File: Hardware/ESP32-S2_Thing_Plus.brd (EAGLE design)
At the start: 22.9 x 64.8 mm, 144 parts, among them J3 QWIIC_RA, J5 USB-C, J6 JTAG, Q1 2.5A/30V, Q2 MBT3904DW1T1, U1 ESP32-S2-WROOM, U2 CP210X, U3 AP2112K-3.3V, U4 MCP73831, U5 TC7USB40MU, Y1 32.768kHz

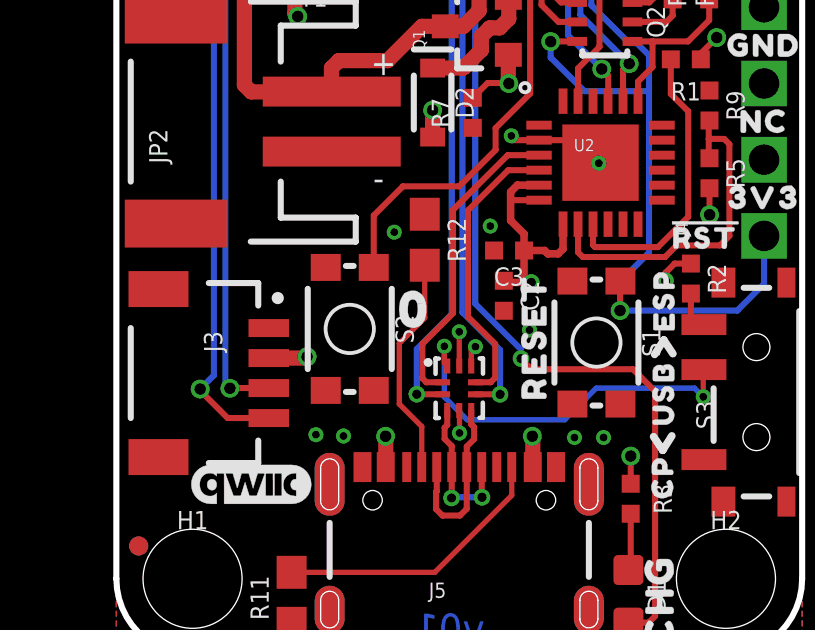
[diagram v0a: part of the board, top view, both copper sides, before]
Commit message: corrected extra IO sch note, moved "0" button to align with reset.
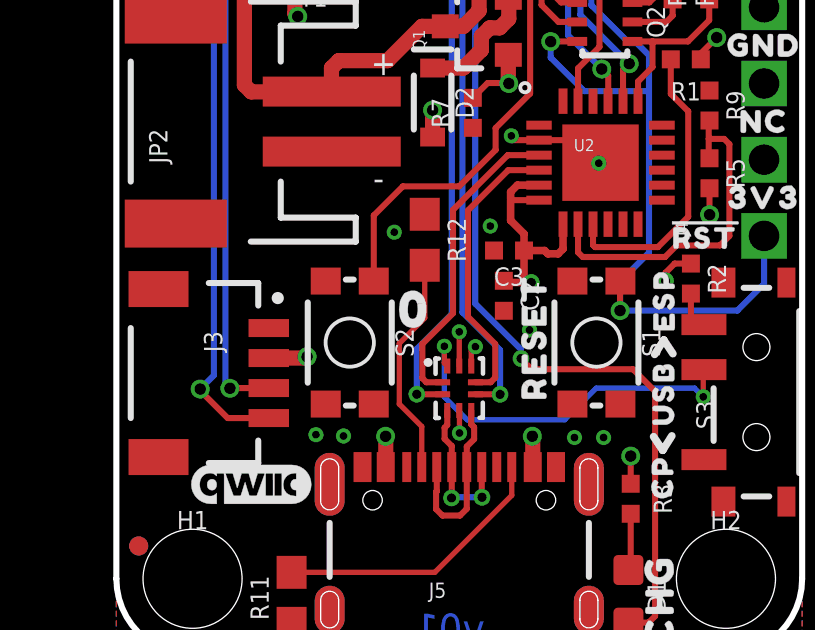
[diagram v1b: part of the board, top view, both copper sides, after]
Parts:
- moved S2 0.45 mm to (7.78, 10.4)
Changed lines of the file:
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@@
 <element name="FD3" library="SparkFun-Aesthetics" package="FIDUCIAL-MICRO" value="FIDUCIALUFIDUCIAL" x="0.74421875" y="3.634740625" smashed="yes"/>
 <element name="FD4" library="SparkFun-Aesthetics" package="FIDUCIAL-MICRO" value="FIDUCIALUFIDUCIAL" x="0.74421875" y="3.634740625" smashed="yes" rot="MR0"/>
-<element name="S2" library="SparkFun-Switches" package="TACTILE_SWITCH_SMD_4.6X2.8MM" value="0" x="7.78001875" y="10.868659375" smashed="yes" rot="R270">
-<attribute name="NAME" x="9.30401875" y="10.868659375" size="0.6096" layer="25" font="vector" ratio="20" rot="R270" align="bottom-center"/>
-<attribute name="PROD_ID" value="SWCH-13065" x="7.78001875" y="10.868659375" size="1.778" layer="27" rot="R270" display="off"/>
-<attribute name="VALUE" x="6.25601875" y="10.868659375" size="0.6096" layer="27" font="vector" ratio="20" rot="R270" align="top-center"/>
+<element name="S2" library="SparkFun-Switches" package="TACTILE_SWITCH_SMD_4.6X2.8MM" value="0" x="7.78001875" y="10.414" smashed="yes" rot="R270">
+<attribute name="NAME" x="9.30401875" y="10.414" size="0.6096" layer="25" font="vector" ratio="20" rot="R270" align="bottom-center"/>
+<attribute name="PROD_ID" value="SWCH-13065" x="7.78001875" y="10.414" size="1.778" layer="27" rot="R270" display="off"/>
+<attribute name="VALUE" x="6.25601875" y="10.414" size="0.6096" layer="27" font="vector" ratio="20" rot="R270" align="top-center"/>
 </element>
 <element name="TP1" library="SparkFun-Connectors" package="TP_15TH" value="" x="17.78" y="24.13" smashed="yes"/>
@@
 <wire x1="11.4274625" y1="15.621" x2="9.5504" y2="15.621" width="0.2032" layer="1"/>
 <wire x1="9.5504" y1="15.621" x2="8.58001875" y2="14.65061875" width="0.2032" layer="1"/>
-<wire x1="8.58001875" y1="14.65061875" x2="8.58001875" y2="12.918659375" width="0.2032" layer="1"/>
+<wire x1="8.58001875" y1="14.65061875" x2="8.58001875" y2="12.464" width="0.2032" layer="1"/>
 <wire x1="13.7922" y1="23.3934" x2="13.7922" y2="18.714721875" width="0.2032" layer="1"/>
 <wire x1="13.7922" y1="18.714721875" x2="12.64158125" y2="17.564103125" width="0.2032" layer="1"/>

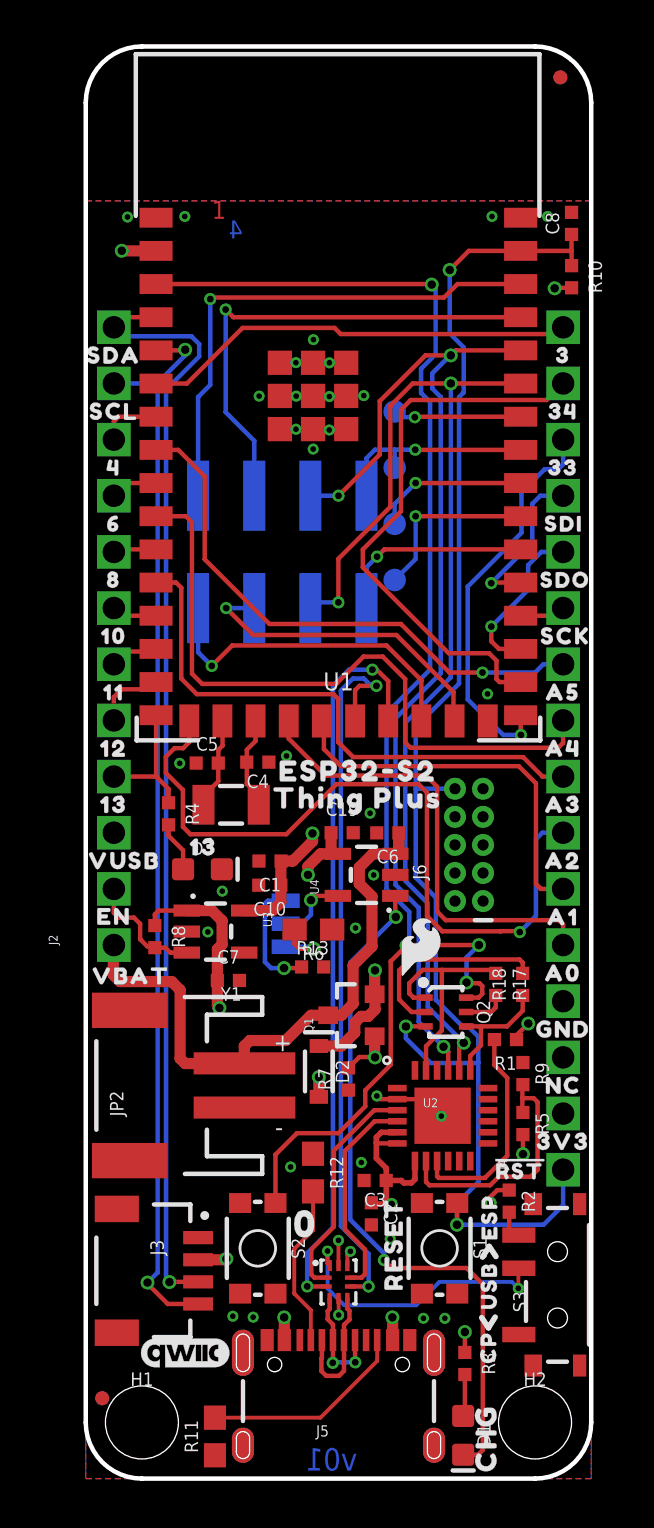
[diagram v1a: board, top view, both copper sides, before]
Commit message: Group design review changes - USB switch to jumper and much more!
-Moved USB selection switch to a 3-way jumper on the bottom.
-Increased Battery + and - label text size
-switched 5.1K resistors to 0402 package
-Moved Charge LED away from standoff
-More GND vias under CP210X
-More GND vias near GND pad on JST batt input
-added pullup on GPIO18 as recommended in datasheet. connected with a NC trace jumper, so user can easily remove if they want. Added big text warning about it in sch.
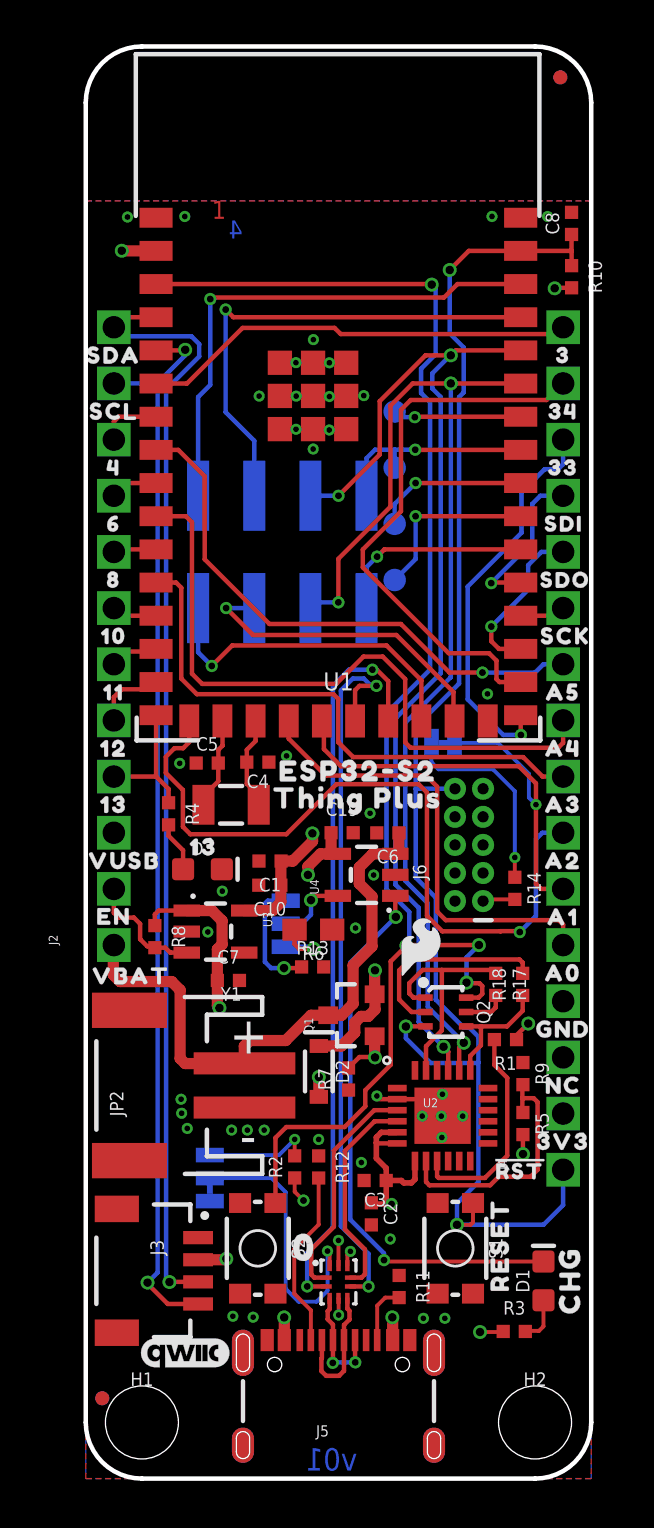
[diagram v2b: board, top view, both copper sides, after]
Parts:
- removed S3: (no value), SparkFun-Switches:SWITCH_SPST_SMD_A
- added GPIO18PU: (no value), SparkFun-Jumpers:SMT-JUMPER_2_NC_TRACE_SILK
- added R14: 10k, SparkFun-Resistors:0402-TIGHT
- added U$9: (no value), output:#ESP32#0
- added USB: (no value), SparkFun-Jumpers:SMT-JUMPER_3_1-NC_TRACE_SILK
- R11, R12: device SparkFun-Resistors:0603 -> SparkFun-Resistors:0402-TIGHT
- U$1: device output:CP0 -> output:#CP210X#0
- U$16: device output:ESP0 -> output:#GPIO18PU#0
- moved U$16 21.6 mm to (15.3, 33.2), flipped to the bottom, turned to 0 degrees
- moved U$1 14.2 mm to (5.54, 12.2), flipped to the bottom
- moved U$14 12.0 mm to (7.34, 13.7), flipped to the bottom
- moved R11 10.7 mm to (14.2, 8.69), turned to 270 degrees
- moved R2 9.83 mm to (9.45, 14.1), turned to 90 degrees
- moved U$78 8.08 mm to (21.9, 8.97)
- moved D1 7.87 mm to (20.7, 8.94), turned to 90 degrees
- moved U$79 4.80 mm to (18.7, 10.6)
- moved R3 2.66 mm to (19.4, 6.65), turned to 0 degrees
- moved U$96 1.07 mm to (9.91, 10.4)
- moved S1 0.71 mm to (16.7, 10.4)
- moved R12 0.36 mm to (10.5, 14.1)
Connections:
- new net N$14: GPIO18PU.2, R14.1
- net 3.3V: now also R14.2
- net A1: now also GPIO18PU.1
- net GND: now also USB.3; no longer S3.3
- net N$6: now also USB.1; no longer S3.1
- net USB_SEL: now also USB.2; no longer S3.2
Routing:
- net N$14: track 0.00 -> 9.08 mm, vias 0 -> 1
- net CC2: track 9.34 -> 2.70 mm
- net CHG: track 31.4 -> 25.2 mm
- net A1: track 17.4 -> 22.9 mm, vias 0 -> 1
- net N$6: track 1.43 -> 4.87 mm, vias 0 -> 1
- net 3.3V: track 32.5 -> 35.3 mm
- net CC1: track 7.39 -> 8.10 mm
- net CHIP_PU: track 68.1 -> 68.7 mm
- net USB_SEL: track 12.8 -> 12.9 mm, vias 2 -> 1
- net GND: vias 33 -> 43

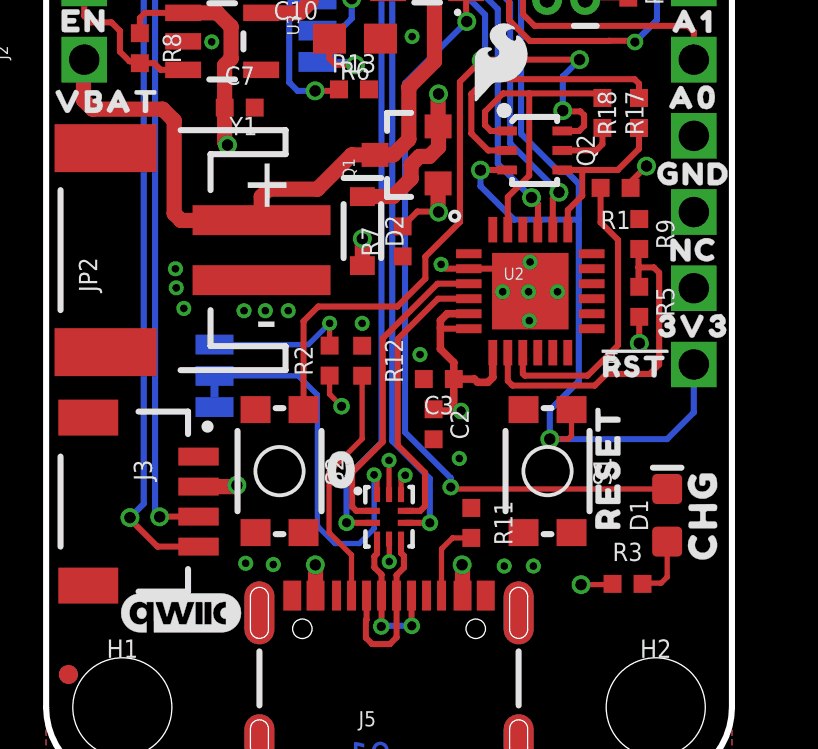
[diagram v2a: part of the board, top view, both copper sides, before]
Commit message: Final changes from groupd proto review (library work)
-Added tNames and tValues to TC7 USB switch IC.
-repositioned tNames and tValues on CP210X footprint.
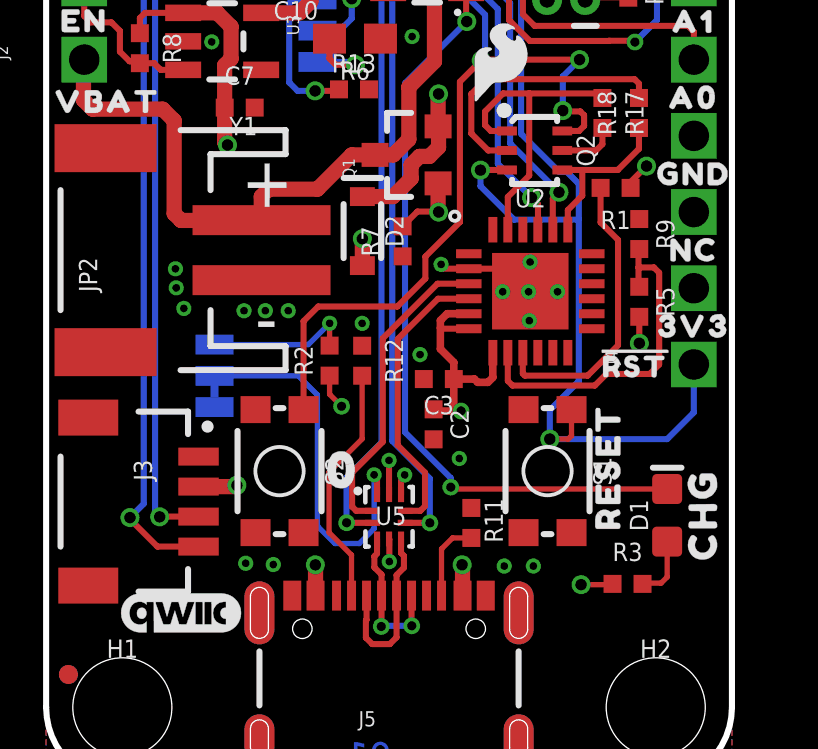
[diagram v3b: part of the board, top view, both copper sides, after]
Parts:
- U3: value AP2112K-3.3V -> AP2112

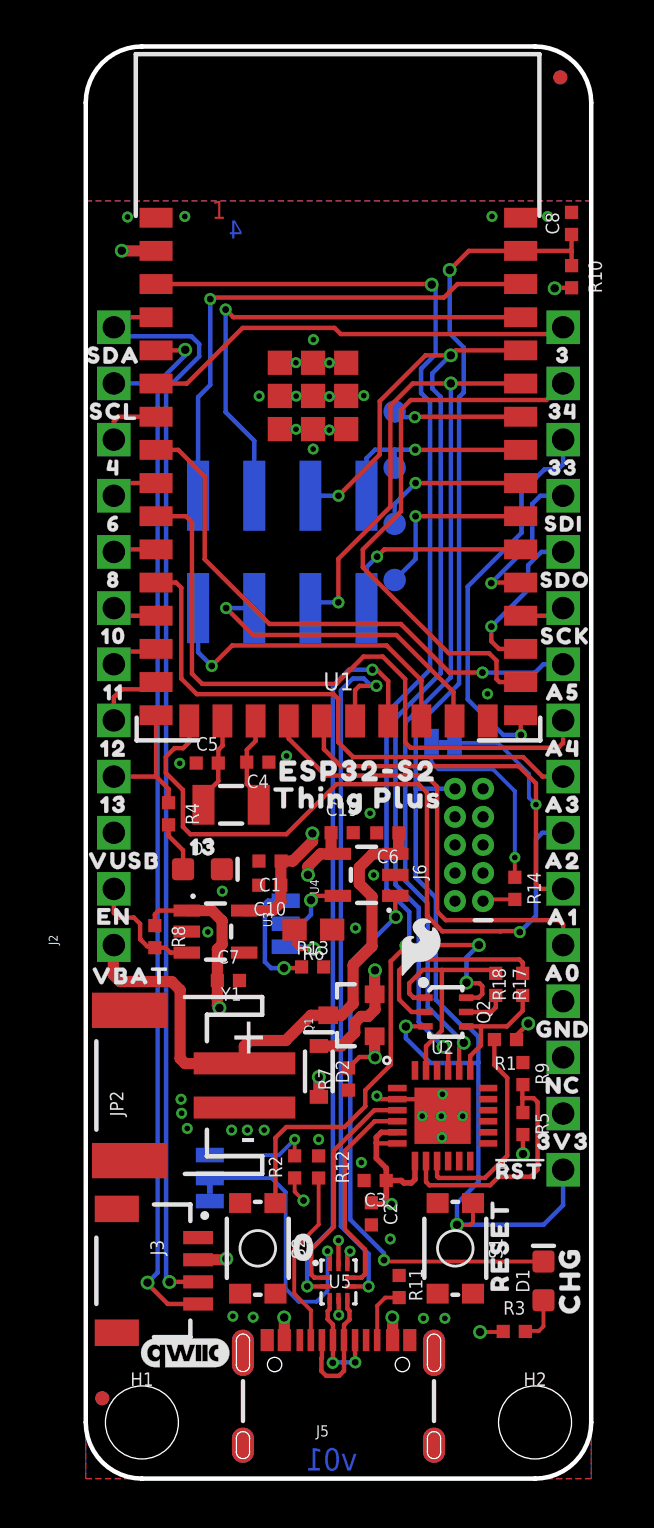
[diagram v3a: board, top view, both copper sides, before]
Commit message: Moved to new DRU, then moved some stuff for better gnd flow
-note, manually kept gnd pour poly isolates at 7/10/10/7, to avoid exposing mask on square pad cornder masks.
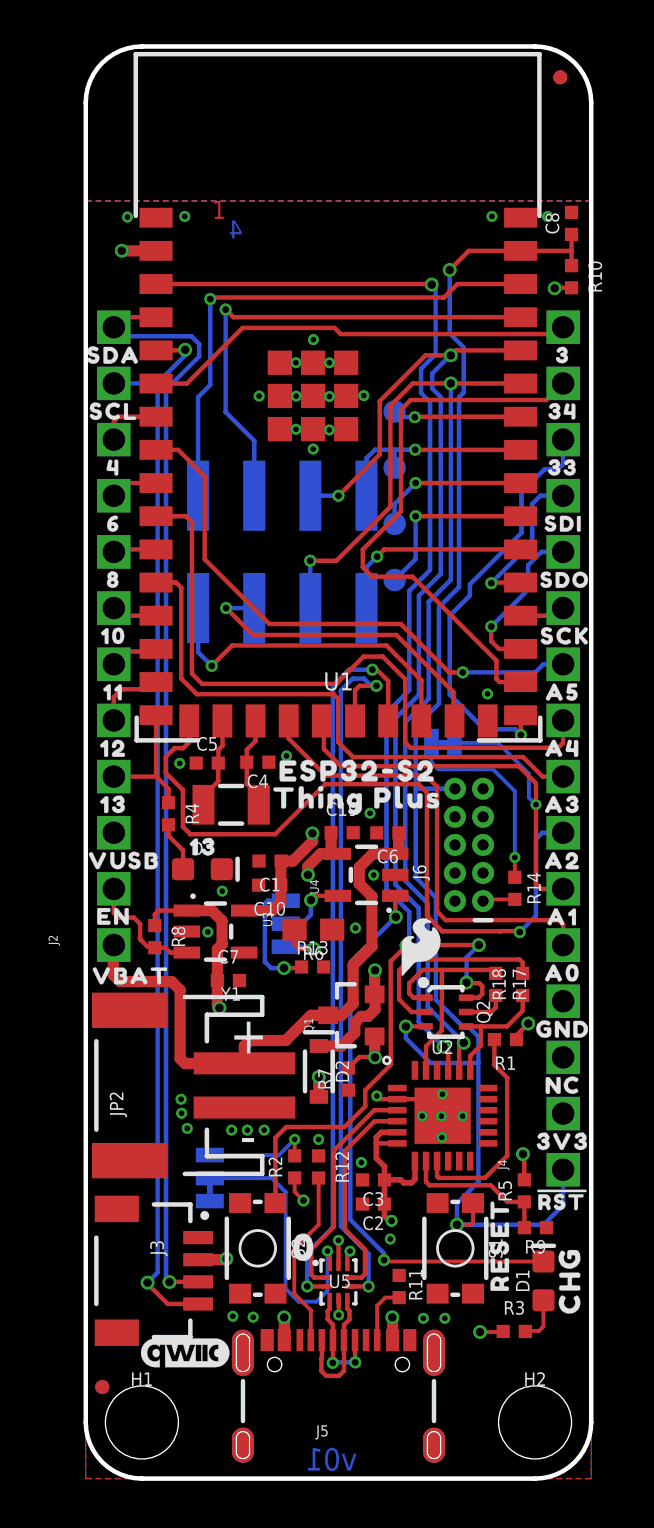
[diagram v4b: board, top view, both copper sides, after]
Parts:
- moved R9 6.99 mm to (20.3, 11.3), turned to 180 degrees
- moved R5 3.05 mm to (19.8, 13.0), turned to 90 degrees
- moved U$7 2.36 mm to (21.5, 12.6)
- moved FD3 0.51 mm to (0.74, 4.14)
- moved FD4 0.51 mm to (0.74, 4.14)
- moved C2 0.45 mm to (13.0, 12.4), turned to 180 degrees
- moved C3 0.08 mm to (13.0, 13.5)
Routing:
- net N$4: track 11.4 -> 6.92 mm
- net 33/RX1: track 17.9 -> 18.9 mm
- net 3.3V: track 35.3 -> 34.6 mm
